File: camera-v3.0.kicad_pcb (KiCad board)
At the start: 2 copper layers, 73.3 x 53.4 mm, 6 parts, among them IC1 USB2660I-JZX-03, IC2 ZXLD1350ET5TA, J1 1775862-2, J2 104031-0811, J3 503960-0696, U1 E73-2G4M08S1C-52840

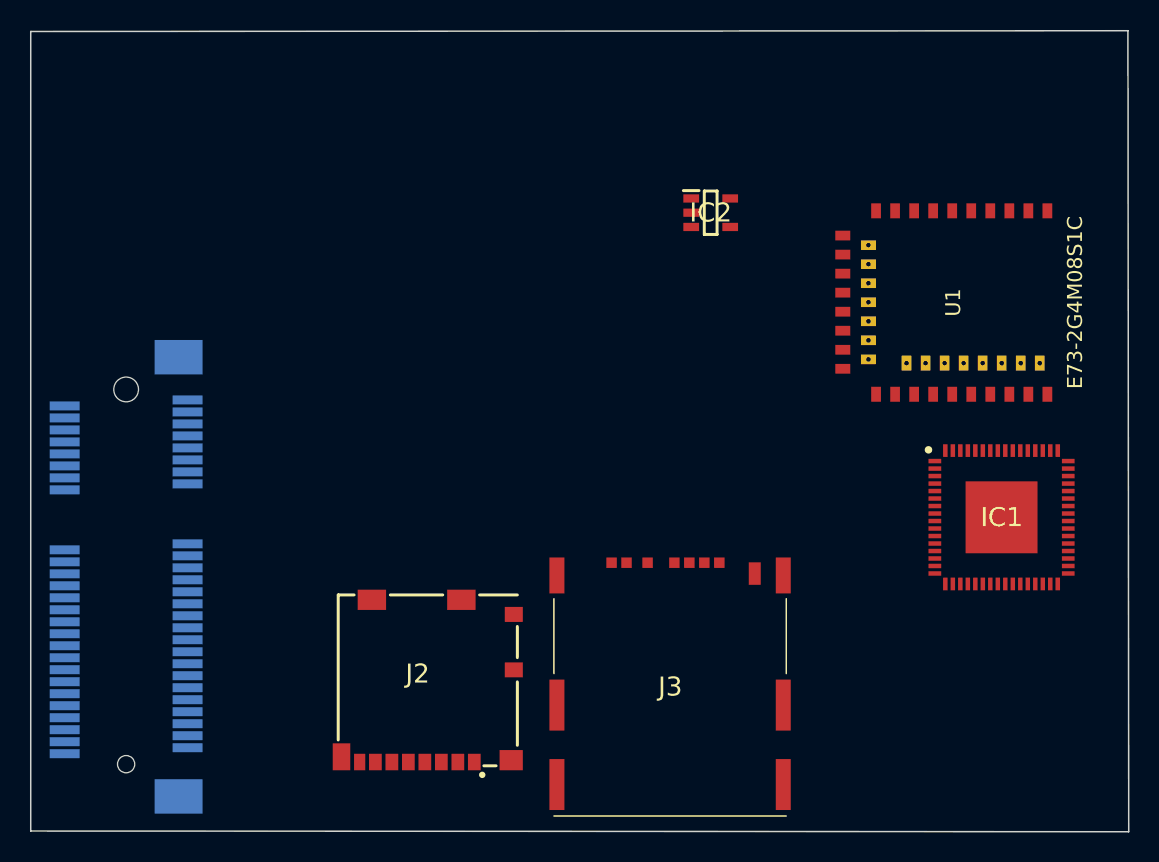
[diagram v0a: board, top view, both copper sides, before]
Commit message: Разработано расположение компонентов
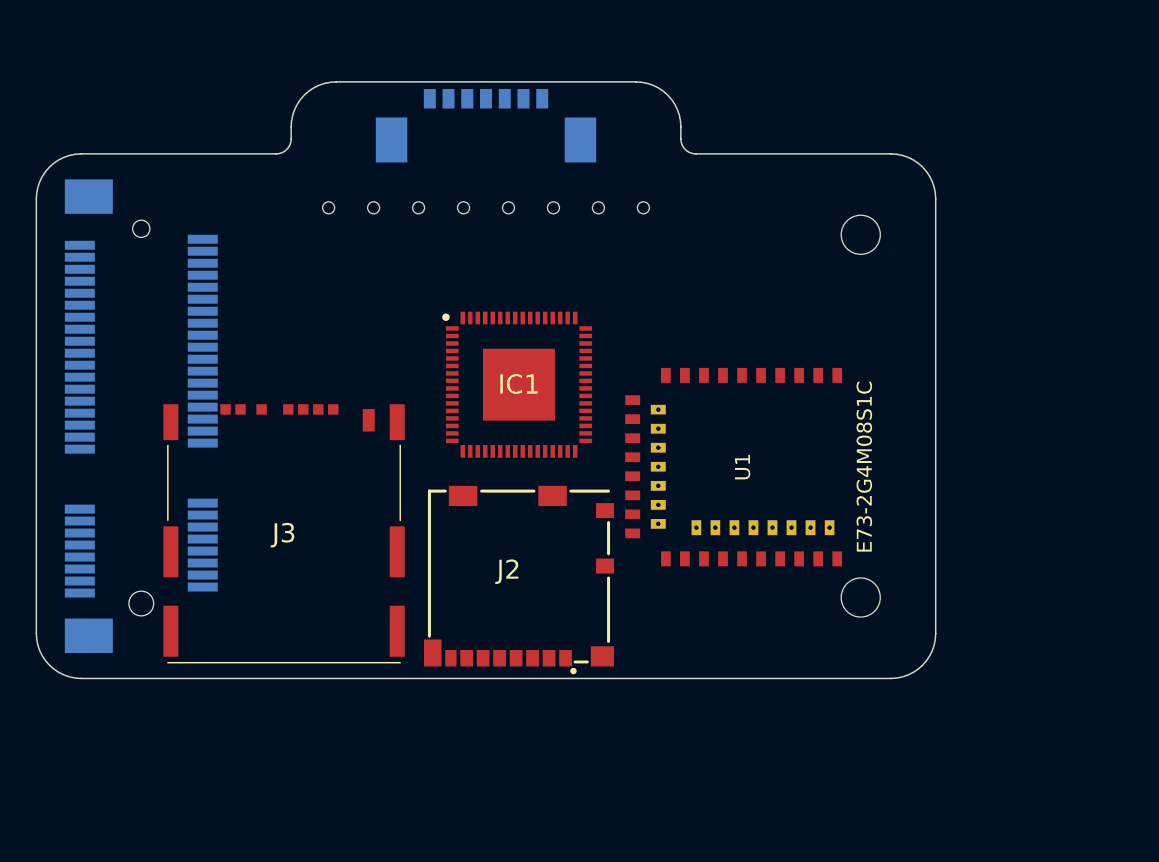
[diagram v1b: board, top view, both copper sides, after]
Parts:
- removed IC2: ZXLD1350ET5TA, mouser:SOT95P280X100-5N
- added J**: 533980771, mouser-local:533980771, B.Cu at (108.1, 69.3)
- moved IC1 33.4 mm to (110.3, 86.2)
- moved J3 27.7 mm to (95.2, 96.3)
- moved U1 17.8 mm to (117.5, 91.7)
- moved J1 10.8 mm to (85.1, 88.3), turned to 90 degrees
- moved J2 9.22 mm to (110.3, 104.7)
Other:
- board size 73.3 x 53.4 mm -> 60 x 39.8 mm

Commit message: 1
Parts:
- added J**: 533980771, mouser-local:533980771, B.Cu at (99.1, 70.1)
- moved J** 9.04 mm to (117.1, 70.1)
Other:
- outline, holes or cut-outs redrawn

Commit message: Добавил ещё компонентов
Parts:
- removed J** (x2): 533980771, mouser-local:533980771
- added J4: 1-1734742-6, mouser-local:117347426, B.Cu at (110.1, 69.7)
- added J5: 1734742-8, mouser-local:17347428, B.Cu at (96.4, 69.6)
- added J6: 53398-0867, mouser-local:533980867, B.Cu at (127.0, 68.7)
- added U2: AXP209, mouser-local:QFN40P600X600X80-49N, F.Cu at (128.2, 80.1)
- J2: footprint mouser:1040310811 -> mouser-local:1040310811
- J3: footprint mouser:5039600696 -> mouser-local:5039600696
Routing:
- net (no net): track 0.00 -> 71.6 mm
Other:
- outline, holes or cut-outs redrawn
